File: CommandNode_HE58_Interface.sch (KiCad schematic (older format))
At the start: 22 parts

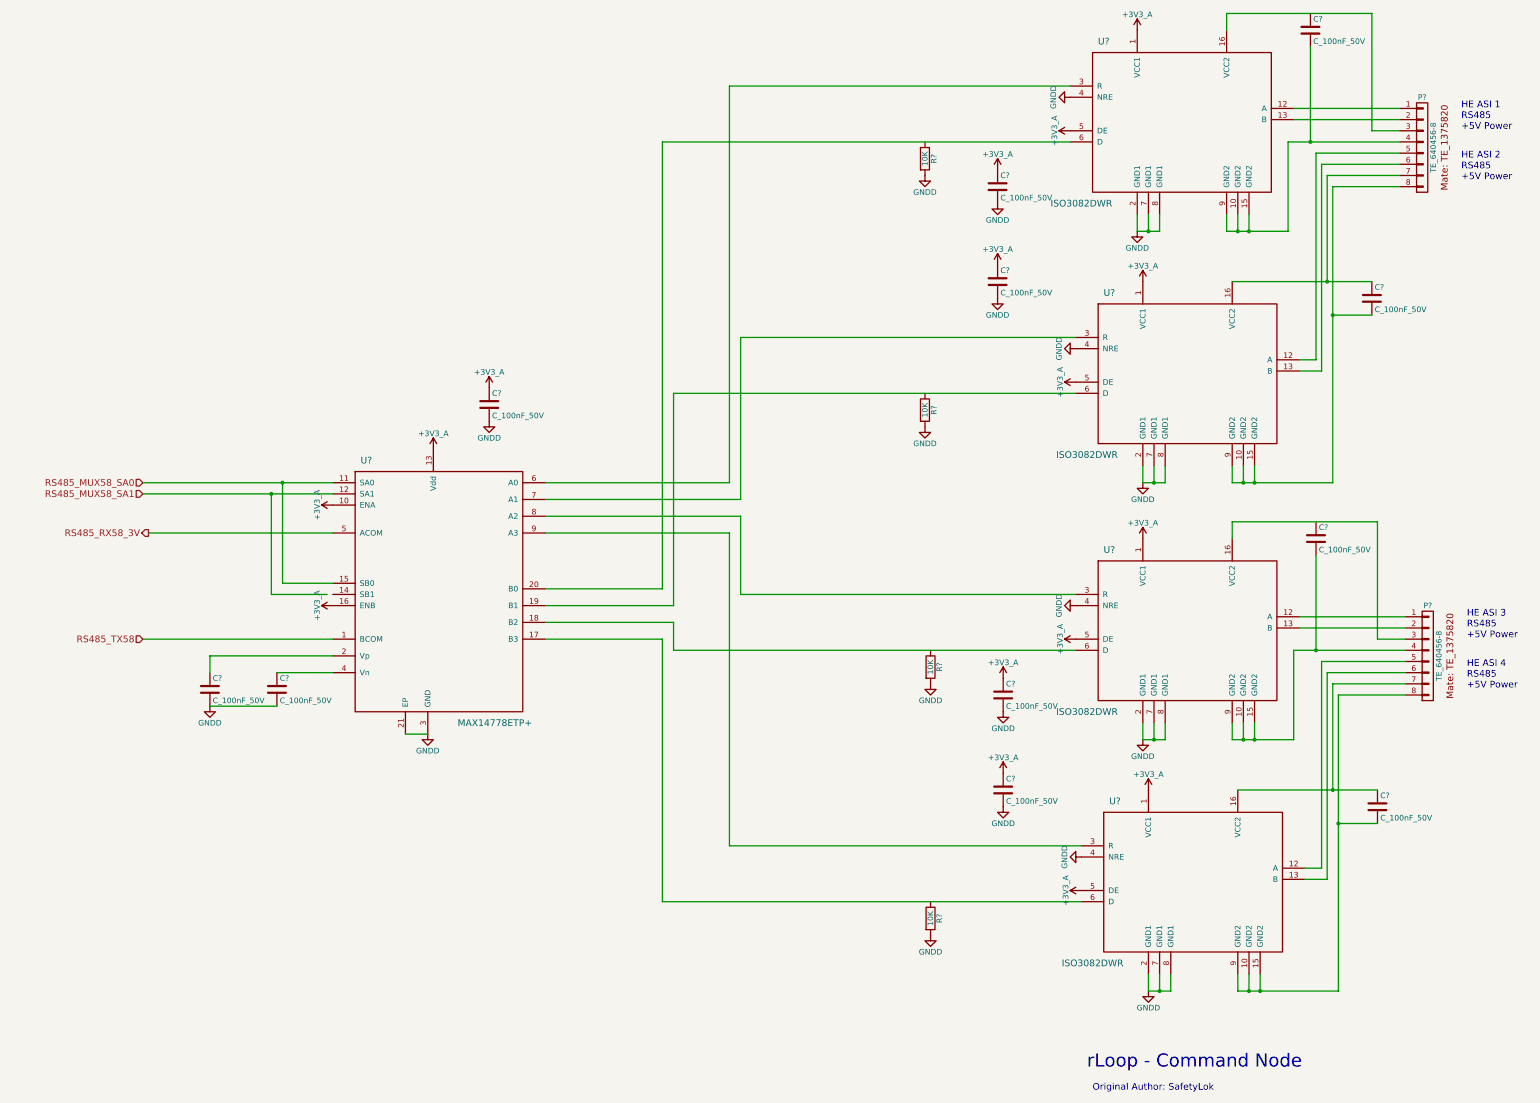
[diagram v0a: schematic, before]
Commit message: Finish and print schematics for review
Lifting mechanism, charger interface, Data Enable on HE controller
RS585, Park Brake and node core.
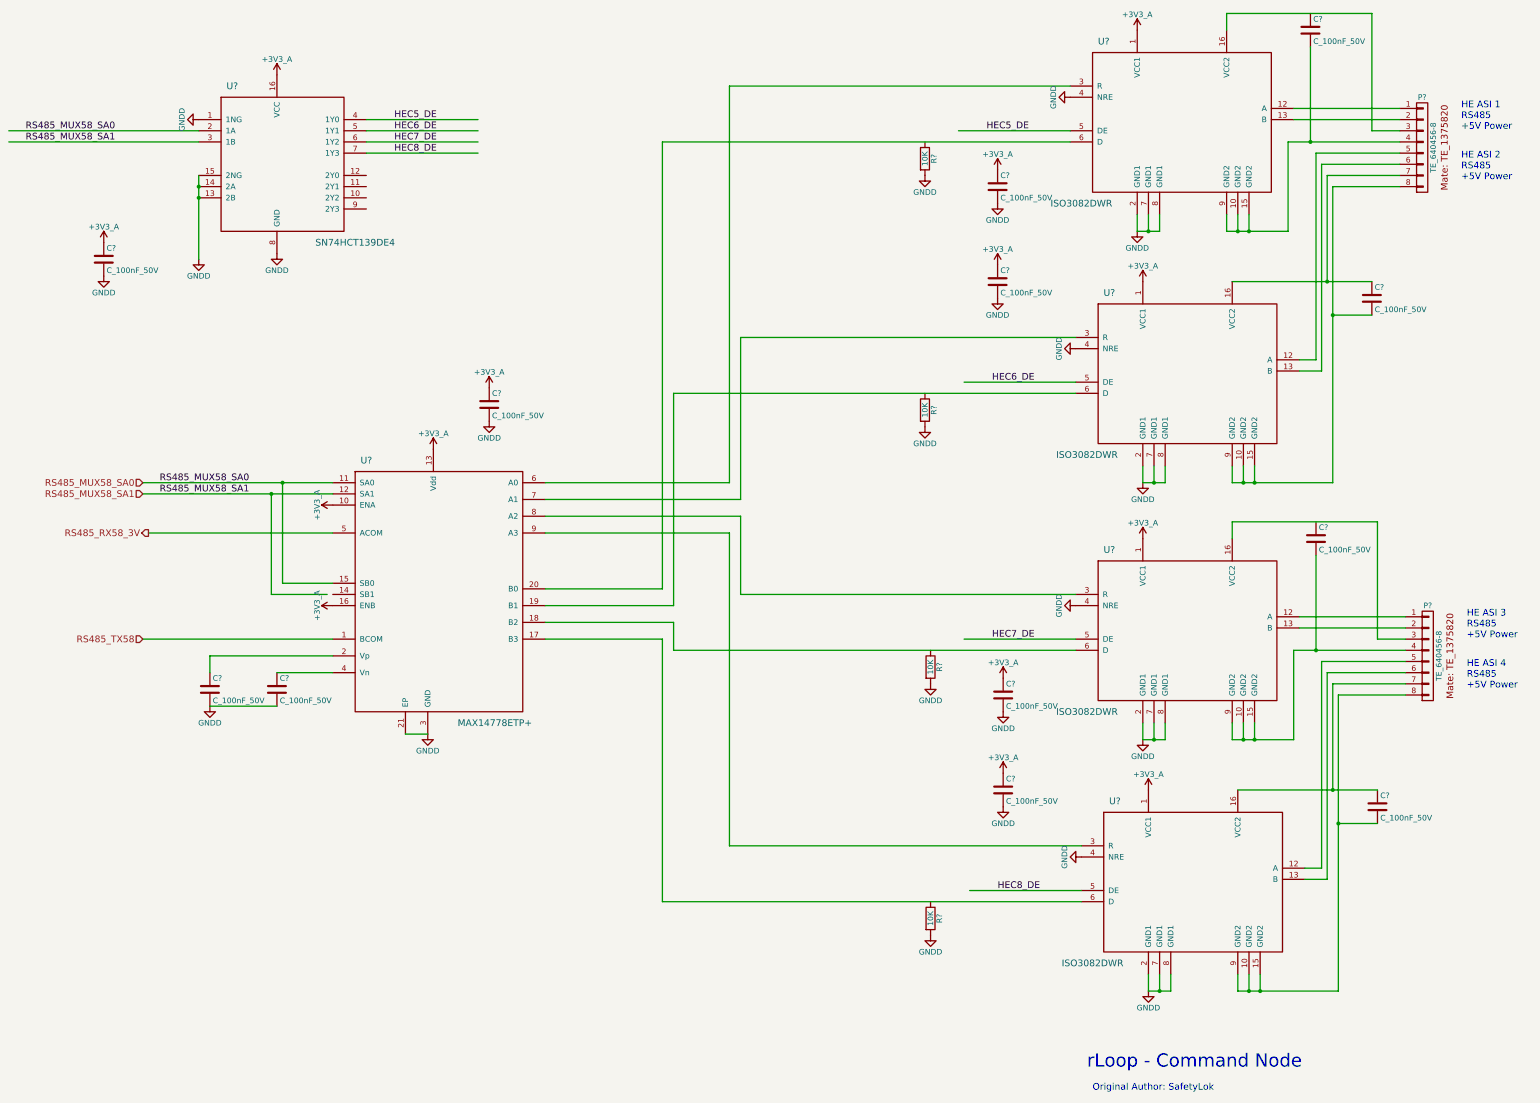
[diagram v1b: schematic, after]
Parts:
- added C?: C_100nF_50V, RLOOP_FOOTPRINTS:rLoop_C_0603, symbol C_100nF_50V
- added U?: SN74HCT139DE4, RLOOP_FOOTPRINTS:rLoop_SOIC_16, symbol SN74HCT139DE4
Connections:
- net labels added: HEC5_DE, HEC6_DE, HEC7_DE, HEC8_DE
- wire segments 111 -> 122
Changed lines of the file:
@@
 $Descr A3 16535 11693
 encoding utf-8
-Sheet 7 7
+Sheet 7 8
 Title "Hover Engine Interface"
 Date ""
@@
 	0    1    1    0
 $EndComp
-$Comp
-L +3V3_A #PWR?
-U 1 1 575D5AC3
-P 11750 1800
-F 0 "#PWR?" H 11750 1650 50  0001 C CNN
-F 1 "+3V3_A" H 11750 1940 50  0000 C CNN
-F 2 "" H 11750 1800 60  0000 C CNN
-F 3 "" H 11750 1800 60  0000 C CNN
-	1    11750 1800
-	0    -1   -1   0
-$EndComp
-$Comp
-L +3V3_A #PWR?
-U 1 1 575D5AC4
-P 11800 4050
-F 0 "#PWR?" H 11800 3900 50  0001 C CNN
-F 1 "+3V3_A" H 11800 4190 50  0000 C CNN
-F 2 "" H 11800 4050 60  0000 C CNN
-F 3 "" H 11800 4050 60  0000 C CNN
-	1    11800 4050
-	0    -1   -1   0
-$EndComp
 Wire Wire Line
 	8200 4150 11800 4150
@@
 	0    1    1    0
 $EndComp
-$Comp
-L +3V3_A #PWR?
-U 1 1 575D5ADA
-P 11800 6350
-F 0 "#PWR?" H 11800 6200 50  0001 C CNN
-F 1 "+3V3_A" H 11800 6490 50  0000 C CNN
-F 2 "" H 11800 6350 60  0000 C CNN
-F 3 "" H 11800 6350 60  0000 C CNN
-	1    11800 6350
-	0    -1   -1   0
-$EndComp
-$Comp
-L +3V3_A #PWR?
-U 1 1 575D5ADB
-P 11850 8600
-F 0 "#PWR?" H 11850 8450 50  0001 C CNN
-F 1 "+3V3_A" H 11850 8740 50  0000 C CNN
-F 2 "" H 11850 8600 60  0000 C CNN
-F 3 "" H 11850 8600 60  0000 C CNN
-	1    11850 8600
-	0    -1   -1   0
-$EndComp
 Wire Wire Line
 	8100 8700 11850 8700
@@
 	4600 5950 4600 5050
 Connection ~ 4600 5050
+$Comp
+L SN74HCT139DE4 U?
+U 1 1 5769F6BC
+P 4150 1500
+F 0 "U?" H 4250 1600 60  0000 C CNN
+F 1 "SN74HCT139DE4" H 5350 200 60  0000 C CNN
+F 2 "RLOOP_FOOTPRINTS:rLoop_SOIC_16" H 4050 1400 60  0001 C CNN
+F 3 "" H 4150 1500 60  0000 C CNN
+	1    4150 1500
+	1    0    0    -1
+$EndComp
+$Comp
+L C_100nF_50V C?
+U 1 1 5769F6C3
+P 3100 2950
+F 0 "C?" H 3125 3050 50  0000 L CNN
+F 1 "C_100nF_50V" H 3125 2850 50  0000 L CNN
+F 2 "RLOOP_FOOTPRINTS:rLoop_C_0603" H 3138 2800 50  0001 C CNN
+F 3 "" H 3100 2950 50  0000 C CNN
+	1    3100 2950
+	1    0    0    -1
+$EndComp
+$Comp
+L GNDD #PWR?
+U 1 1 5769F6CA
+P 3100 3100
+F 0 "#PWR?" H 3100 2850 50  0001 C CNN
+F 1 "GNDD" H 3100 2950 50  0000 C CNN
+F 2 "" H 3100 3100 50  0000 C CNN
+F 3 "" H 3100 3100 50  0000 C CNN
+	1    3100 3100
+	1    0    0    -1
+$EndComp
+$Comp
+L +3V3_A #PWR?
+U 1 1 5769F6D0
+P 3100 2800
+F 0 "#PWR?" H 3100 2650 50  0001 C CNN
+F 1 "+3V3_A" H 3100 2940 50  0000 C CNN
+F 2 "" H 3100 2800 60  0000 C CNN
+F 3 "" H 3100 2800 60  0000 C CNN
+	1    3100 2800
+	1    0    0    -1
+$EndComp
+$Comp
+L GNDD #PWR?
+U 1 1 5769F6D6
+P 4650 2900
+F 0 "#PWR?" H 4650 2650 50  0001 C CNN
+F 1 "GNDD" H 4650 2750 50  0000 C CNN
+F 2 "" H 4650 2900 50  0000 C CNN
+F 3 "" H 4650 2900 50  0000 C CNN
+	1    4650 2900
+	1    0    0    -1
+$EndComp
+$Comp
+L +3V3_A #PWR?
+U 1 1 5769F6DC
+P 4650 1300
+F 0 "#PWR?" H 4650 1150 50  0001 C CNN
+F 1 "+3V3_A" H 4650 1440 50  0000 C CNN
+F 2 "" H 4650 1300 60  0000 C CNN
+F 3 "" H 4650 1300 60  0000 C CNN
+	1    4650 1300
+	1    0    0    -1
+$EndComp
+$Comp
+L GNDD #PWR?
+U 1 1 5769F6E2
+P 3950 2950
+F 0 "#PWR?" H 3950 2700 50  0001 C CNN
+F 1 "GNDD" H 3950 2800 50  0000 C CNN
+F 2 "" H 3950 2950 50  0000 C CNN
+F 3 "" H 3950 2950 50  0000 C CNN
+	1    3950 2950
+	1    0    0    -1
+$EndComp
+Wire Wire Line
+	3950 2200 3950 2950
+Connection ~ 3950 2300
+Connection ~ 3950 2400
+Wire Wire Line
+	5450 1800 6450 1800
+Text Label 5700 1800 0    60   ~ 0
+HEC6_DE
+Wire Wire Line
+	5450 1900 6450 1900
+Text Label 5700 1900 0    60   ~ 0
+HEC7_DE
+Wire Wire Line
+	5450 2000 6450 2000
+Text Label 5700 2000 0    60   ~ 0
+HEC8_DE
+$Comp
+L GNDD #PWR?
+U 1 1 5769F6F5
+P 3950 1700
+F 0 "#PWR?" H 3950 1450 50  0001 C CNN
+F 1 "GNDD" H 3950 1550 50  0000 C CNN
+F 2 "" H 3950 1700 50  0000 C CNN
+F 3 "" H 3950 1700 50  0000 C CNN
+	1    3950 1700
+	0    1    1    0
+$EndComp
+Text Label 3600 4950 0    60   ~ 0
+RS485_MUX58_SA0
+Text Label 3600 5050 0    60   ~ 0
+RS485_MUX58_SA1
+Wire Wire Line
+	2250 1800 3950 1800
+Wire Wire Line
+	2250 1900 3950 1900
+Text Label 2400 1800 0    60   ~ 0
+RS485_MUX58_SA0
+Text Label 2400 1900 0    60   ~ 0
+RS485_MUX58_SA1
+Wire Wire Line
+	5450 1700 6450 1700
+Text Label 5700 1700 0    60   ~ 0
+HEC5_DE
+Wire Wire Line
+	10800 4050 11800 4050
+Text Label 11050 4050 0    60   ~ 0
+HEC6_DE
+Wire Wire Line
+	10800 6350 11800 6350
+Text Label 11050 6350 0    60   ~ 0
+HEC7_DE
+Wire Wire Line
+	10850 8600 11850 8600
+Text Label 11100 8600 0    60   ~ 0
+HEC8_DE
+Wire Wire Line
+	10750 1800 11750 1800
+Text Label 11000 1800 0    60   ~ 0
+HEC5_DE
 $EndSCHEMATC
